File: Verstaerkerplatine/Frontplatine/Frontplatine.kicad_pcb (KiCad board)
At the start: 2 copper layers, 99.1 x 99.1 mm, 38 parts, among them J1 GND, J10 IV_IN_+, J11 IV_OUT, J12 IV_REF, J13 AVS_IN_+, J14 AVS_IN_-, J16 A0, J17 A1, J18 A2, J19 A3, J20 GND, J21 -5V, J22 3.3V, J23 5V, J24 DI_IN_2, J25 DI_IN_1, J26 DI_OUT_3, J27 DI_OUT_2, J28 DI_OUT_1, J29 EM_20, J3 EM_OUT, J30 LED_20, J31 D/A_+, J32 5V_BUS, J33 3.3V_BUS, J34 EM_KOND, J4 GND_EM, J5 EM_IN, J6 PW_IN, J7 PW_OUT, J8 REF, J9 IV_IN_-

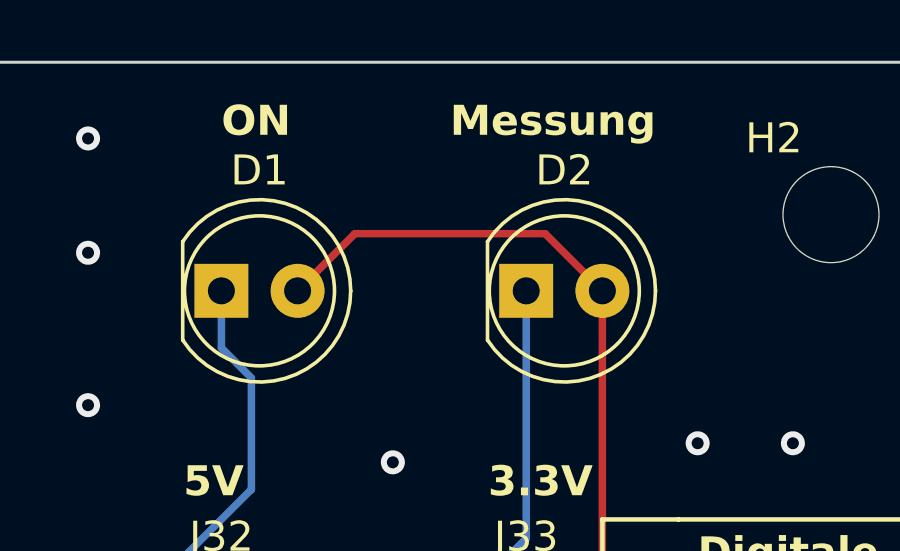
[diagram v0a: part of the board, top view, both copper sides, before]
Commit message: LED connection moved
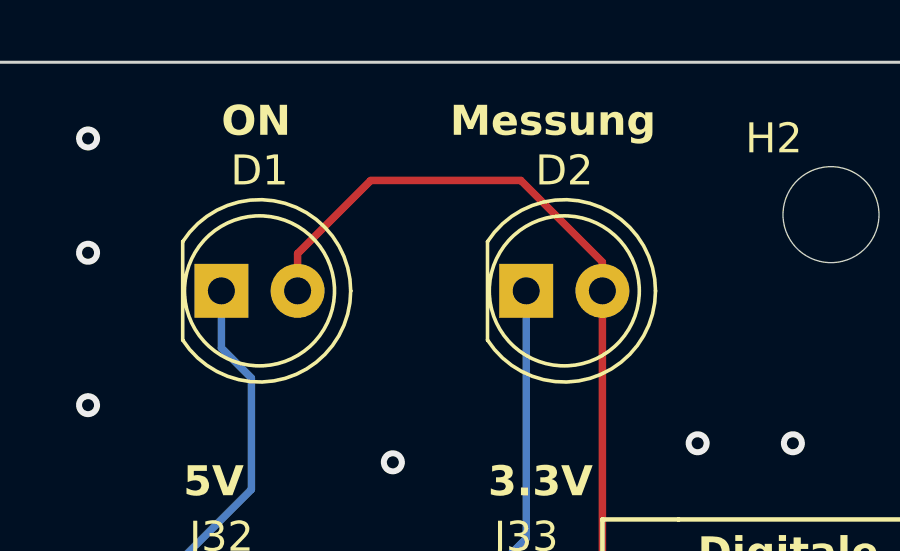
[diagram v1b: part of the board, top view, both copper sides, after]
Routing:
- net +3.3V: track 201.5 -> 204.3 mm
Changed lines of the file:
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@@
+	)
+	(segment
+		(start 165 39.5)
+		(end 170 39.5)
+		(width 0.25)
+		(layer "F.Cu")
+		(net 2)
 	)
 	(segment
@@
 	)
 	(segment
+		(start 170 39.5)
+		(end 172.72 42.22)
+		(width 0.25)
+		(layer "F.Cu")
+		(net 2)
+	)
+	(segment
 		(start 172.72 43.18)
 		(end 172.72 53.34)
@@
 	)
 	(segment
-		(start 164.465 41.275)
-		(end 170.815 41.275)
-		(width 0.25)
-		(layer "F.Cu")
-		(net 2)
-	)
-	(segment
-		(start 162.56 43.18)
-		(end 164.465 41.275)
-		(width 0.25)
-		(layer "F.Cu")
-		(net 2)
-	)
-	(segment
 		(start 171.45 85.725)
 		(end 171.45 57.15)
-		(width 0.25)
-		(layer "F.Cu")
-		(net 2)
-	)
-	(segment
-		(start 170.815 41.275)
-		(end 172.72 43.18)
 		(width 0.25)
 		(layer "F.Cu")
@@
 		(width 0.25)
 		(layer "F.Cu")
+		(net 2)
+	)
+	(segment
+		(start 172.72 42.22)
+		(end 172.72 43.18)
+		(width 0.25)
+		(layer "F.Cu")
+		(net 2)
+	)
+	(segment
+		(start 162.56 41.94)
+		(end 165 39.5)
+		(width 0.25)
+		(layer "F.Cu")
+		(net 2)
+	)
+	(segment
+		(start 162.56 43.18)
+		(end 162.56 41.94)
+		(width 0.25)
+		(layer "F.Cu")

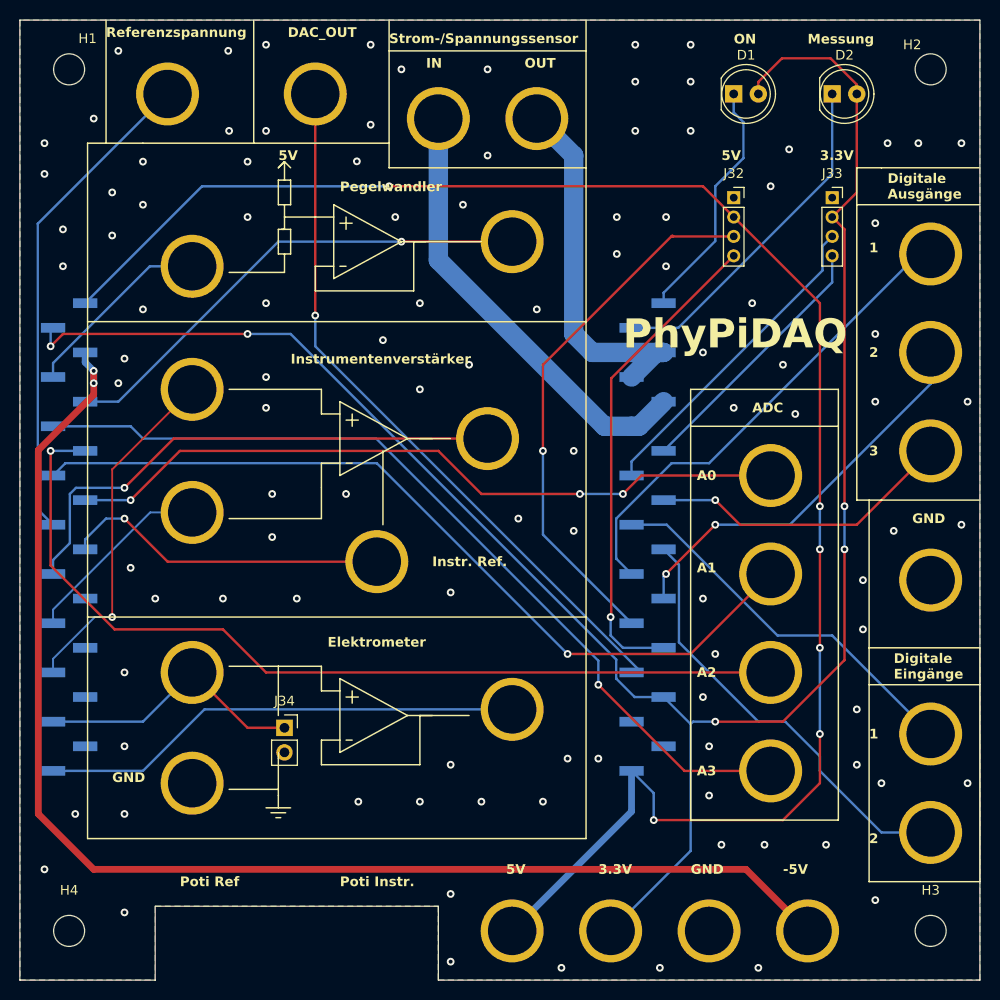
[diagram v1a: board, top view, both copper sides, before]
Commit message: wired connection for CA3140 in and IN219 IN+ and IN-
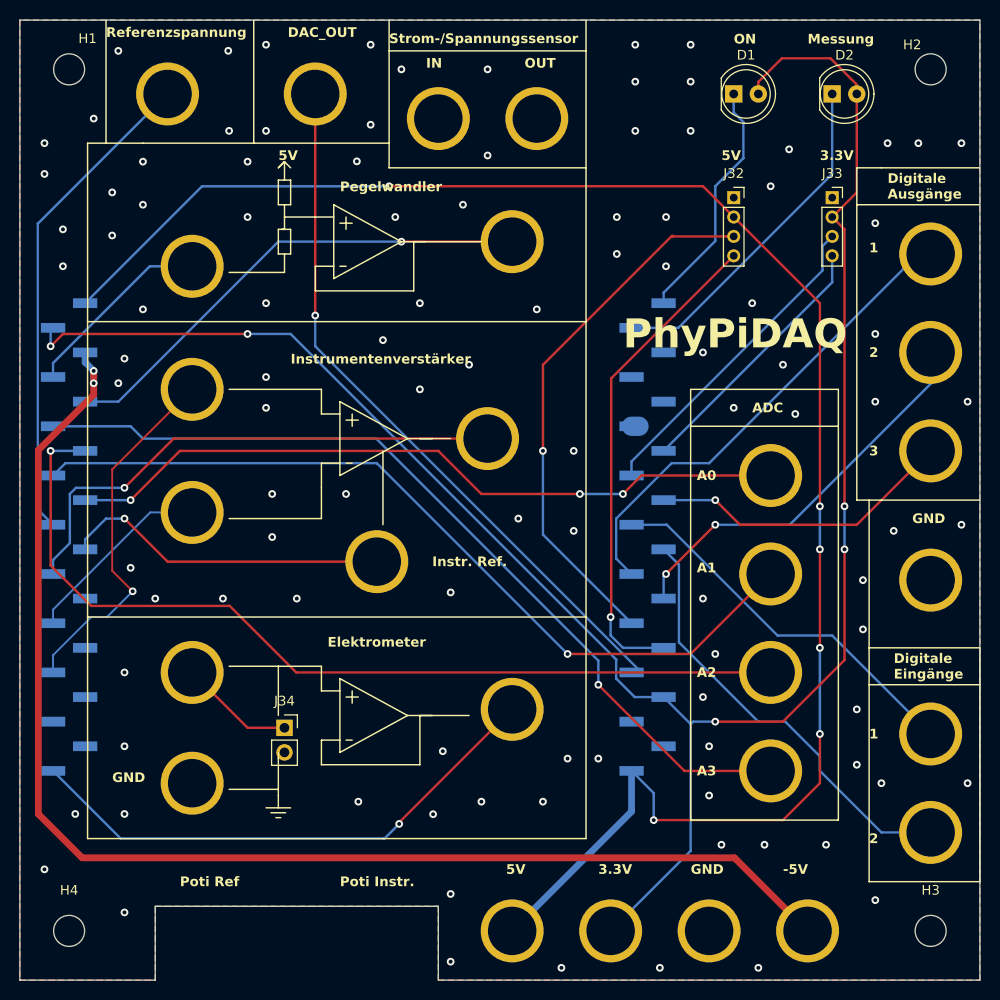
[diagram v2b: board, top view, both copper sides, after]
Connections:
- J13 pad 1: StromSpannungsSensor_IN_+ -> unconnected-(J13-Pin_1-Pad1)
- J14 pad 1: StromSpannungsSensor_IN_- -> unconnected-(J14-Pin_1-Pad1)
- J29 pad 3: Elektrometer_IN_+ -> unconnected-(J29-Pin_3-Pad3)
- J30 pad 3: StromSpannungsSensor_IN_- -> unconnected-(J30-Pin_3-Pad3)
- J30 pad 4: StromSpannungsSensor_IN_- -> unconnected-(J30-Pin_4-Pad4)
- J30 pad 5: StromSpannungsSensor_IN_+ -> unconnected-(J30-Pin_5-Pad5)
- J30 pad 6: StromSpannungsSensor_IN_+ -> unconnected-(J30-Pin_6-Pad6)
- J34 pad 1: Elektrometer_IN_+ -> Net-(J34-Pin_1)
- J5 pad 1: Elektrometer_IN_+ -> Net-(J34-Pin_1)
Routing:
- net StromSpannungsSensor_IN_+: track 46.0 -> 0.00 mm
- net StromSpannungsSensor_IN_-: track 38.2 -> 0.00 mm
- net Elektrometer_IN_+: track 28.4 -> 0.00 mm
- net Net-(J34-Pin_1): track 0.00 -> 11.9 mm
- net Elektrometer_OUT: track 50.0 -> 55.9 mm, vias 0 -> 1
- net Instrumentenverstaerker_IN_+: track 36.2 -> 37.9 mm
- net unconnected-(J30-Pin_6-Pad6): track 0.00 -> 0.77 mm
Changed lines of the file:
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@@
 	(net 4 "GND")
 	(net 5 "Elektrometer_OUT")
-	(net 6 "Elektrometer_IN_+")
+	(net 6 "Net-(J34-Pin_1)")
 	(net 7 "Pegelwandler_IN_+")
 	(net 8 "Pegelwandler_OUT")
@@
 	(net 12 "Instrumentenverstaerker_OUT")
 	(net 13 "Instrumentenverstaerker_Ref")
-	(net 14 "StromSpannungsSensor_IN_+")
-	(net 15 "StromSpannungsSensor_IN_-")
+	(net 14 "unconnected-(J13-Pin_1-Pad1)")
+	(net 15 "unconnected-(J14-Pin_1-Pad1)")
 	(net 16 "A0")
 	(net 17 "A1")
@@
 	(net 30 "SCL_5")
 	(net 31 "DAC_OUT")
+	(net 32 "unconnected-(J29-Pin_3-Pad3)")
+	(net 33 "unconnected-(J30-Pin_5-Pad5)")
+	(net 34 "unconnected-(J30-Pin_4-Pad4)")
+	(net 35 "unconnected-(J30-Pin_3-Pad3)")
+	(net 36 "unconnected-(J30-Pin_6-Pad6)")
 	(footprint "MountingHole:MountingHole_3.2mm_M3"
 		(layer "F.Cu")
@@
 			(layers "*.Cu" "*.Mask")
 			(remove_unused_layers no)
-			(net 6 "Elektrometer_IN_+")
+			(net 6 "Net-(J34-Pin_1)")
 			(pinfunction "Pin_1")
 			(pintype "passive")
@@
 			(layers "*.Cu" "*.Mask")
 			(remove_unused_layers no)
-			(net 14 "StromSpannungsSensor_IN_+")
+			(net 14 "unconnected-(J13-Pin_1-Pad1)")
 			(pinfunction "Pin_1")
 			(pintype "passive")
@@
 			(layers "*.Cu" "*.Mask")
 			(remove_unused_layers no)
-			(net 6 "Elektrometer_IN_+")
+			(net 6 "Net-(J34-Pin_1)")
 			(pinfunction "Pin_1")
 			(pintype "passive")
@@
 			(size 2.51 1)
 			(layers "B.Cu" "B.Mask" "B.Paste")
-			(net 6 "Elektrometer_IN_+")
+			(net 32 "unconnected-(J29-Pin_3-Pad3)")
 			(pinfunction "Pin_3")
-			(pintype "passive")
+			(pintype "passive+no_connect")
 		)
 		(pad "4" smd rect
@@
 			(layers "*.Cu" "*.Mask")
 			(remove_unused_layers no)
-			(net 15 "StromSpannungsSensor_IN_-")
+			(net 15 "unconnected-(J14-Pin_1-Pad1)")
 			(pinfunction "Pin_1")
 			(pintype "passive")
@@
 			(size 2.51 1)
 			(layers "B.Cu" "B.Mask" "B.Paste")
-			(net 15 "StromSpannungsSensor_IN_-")
+			(net 35 "unconnected-(J30-Pin_3-Pad3)")
 			(pinfunction "Pin_3")
-			(pintype "passive")
+			(pintype "passive+no_connect")
 		)
 		(pad "4" smd rect
@@
 			(size 2.51 1)
 			(layers "B.Cu" "B.Mask" "B.Paste")
-			(net 15 "StromSpannungsSensor_IN_-")
+			(net 34 "unconnected-(J30-Pin_4-Pad4)")
 			(pinfunction "Pin_4")
-			(pintype "passive")
+			(pintype "passive+no_connect")
 		)
 		(pad "5" smd rect
@@
 			(size 2.51 1)
 			(layers "B.Cu" "B.Mask" "B.Paste")
-			(net 14 "StromSpannungsSensor_IN_+")
+			(net 33 "unconnected-(J30-Pin_5-Pad5)")
 			(pinfunction "Pin_5")
-			(pintype "passive")
+			(pintype "passive+no_connect")
 		)
 		(pad "6" smd rect
@@
 			(size 2.51 1)
 			(layers "B.Cu" "B.Mask" "B.Paste")
-			(net 14 "StromSpannungsSensor_IN_+")
+			(net 36 "unconnected-(J30-Pin_6-Pad6)")
 			(pinfunction "Pin_6")
-			(pintype "passive")
+			(pintype "passive+no_connect")
 		)
 		(pad "7" smd rect
@@
 	)
 	(via
-		(at 127.635 116.205)
+		(at 129 117.5)
 		(size 0.8)
 		(drill 0.4)
@@
 	)
 	(via
-		(at 130.81 112.395)
+		(at 130 111)
 		(size 0.8)
 		(drill 0.4)
@@
 	)
 	(segment
-		(start 99.06 113.03)
-		(end 105.41 106.68)
+		(start 125.5 118.5)
+		(end 125.5 118.34)
 		(width 0.25)
-		(layer "B.Cu")
+		(layer "F.Cu")
 		(net 5)
 	)
 	(segment
-		(start 105.41 106.68)
+		(start 125.5 118.34)
 		(end 137.16 106.68)
 		(width 0.25)
+		(layer "F.Cu")
+		(net 5)
+	)
+	(via
+		(at 125.5 118.5)
+		(size 0.8)
+		(drill 0.4)
+		(layers "F.Cu" "B.Cu")
+		(net 5)
+	)
+	(segment
+		(start 124 120)
+		(end 125.5 118.5)
+		(width 0.25)
+		(layer "B.Cu")
+		(net 5)
+	)
+	(segment
+		(start 96.755 120)
+		(end 123.84 120)
+		(width 0.25)
+		(layer "B.Cu")
+		(net 5)
+	)
+	(segment
+		(start 123.84 120)
+		(end 124 120)
+		(width 0.25)
 		(layer "B.Cu")
 		(net 5)
@@
 	(segment
 		(start 89.785 113.03)
-		(end 99.06 113.03)
+		(end 96.755 120)
 		(width 0.25)
 		(layer "B.Cu")
@@
 	)
 	(segment
-		(start 89.785 107.95)
-		(end 99.06 107.95)
-		(width 0.25)
-		(layer "B.Cu")
-		(net 6)
-	)
-	(segment
-		(start 99.06 107.95)
-		(end 104.14 102.87)
-		(width 0.25)
-		(layer "B.Cu")
-		(net 6)
-	)
-	(segment
 		(start 89.785 72.39)
 		(end 89.785 70.94538)
@@
 	)
 	(segment
-		(start 104.14 73.66)
+		(start 95.885 92.385)
 		(end 95.885 81.915)
 		(width 0.2)
@@
 	)
 	(segment
+		(start 98 94.5)
+		(end 95.885 92.385)
+		(width 0.2)
+		(layer "F.Cu")
+		(net 11)
+	)
+	(segment
 		(start 95.885 81.915)
-		(end 95.885 97.155)
+		(end 104.14 73.66)
 		(width 0.2)
 		(layer "F.Cu")
@@
 	)
 	(via
-		(at 95.885 97.155)
+		(at 98 94.5)
 		(size 0.8)
 		(drill 0.4)
@@
 	)
 	(segment
-		(start 95.885 97.155)
-		(end 94.090736 97.155)
+		(start 95.345 97.155)
+		(end 93.717868 97.155)
 		(width 0.2)
 		(layer "B.Cu")
@@
 	)
 	(segment
-		(start 89.785 101.460736)
-		(end 89.785 102.87)
+		(start 93.717868 97.155)
+		(end 89.785 101.087868)
 		(width 0.2)
 		(layer "B.Cu")
@@
 	)
 	(segment
-		(start 94.090736 97.155)
-		(end 89.785 101.460736)
+		(start 98 94.5)
+		(end 95.345 97.155)
+		(width 0.2)
+		(layer "B.Cu")
+		(net 11)
+	)
+	(segment
+		(start 89.785 101.087868)
+		(end 89.785 102.87)
 		(width 0.2)
 		(layer "B.Cu")
@@
 	)
 	(segment
-		(start 149.475 77.47)
-		(end 150.245 77.47)
-		(width 2)
-		(layer "B.Cu")
-		(net 14)
-	)
-	(segment
-		(start 146.685 77.47)
-		(end 129.54 60.325)
-		(width 2)
-		(layer "B.Cu")
-		(net 14)
-	)
-	(segment
-		(start 150.245 77.47)
-		(end 152.785 74.93)
-		(width 2)
-		(layer "B.Cu")
-		(net 14)
-	)
-	(segment
-		(start 149.475 77.47)
-		(end 146.685 77.47)
-		(width 2)
-		(layer "B.Cu")
-		(net 14)
-	)
-	(segment
-		(start 129.54 60.325)
-		(end 129.54 45.72)
-		(width 2)
-		(layer "B.Cu")
-		(net 14)
-	)
-	(segment
-		(start 152.015 69.85)
-		(end 149.475 72.39)
-		(width 2)
-		(layer "B.Cu")
-		(net 15)
-	)
-	(segment
-		(start 145.415 69.85)
-		(end 143.51 67.945)
-		(width 2)
-		(layer "B.Cu")
-		(net 15)
-	)
-	(segment
-		(start 152.785 69.85)
-		(end 145.415 69.85)
-		(width 2)
-		(layer "B.Cu")
-		(net 15)
-	)
-	(segment
-		(start 143.51 67.945)
-		(end 143.51 49.53)
-		(width 2)
-		(layer "B.Cu")
-		(net 15)
-	)
-	(segment
-		(start 152.785 69.85)
-		(end 152.015 69.85)
-		(width 2)
-		(layer "B.Cu")
-		(net 15)
-	)
-	(segment
-		(start 143.51 49.53)
-		(end 139.7 45.72)
-		(width 2)
-		(layer "B.Cu")
-		(net 15)
-	)
-	(segment
 		(start 97.79 85.09)
 		(end 102.87 80.01)
@@
 	)
 	(segment
-		(start 89.535 91.830305)
-		(end 89.535 80.01)
+		(start 108 96)
+		(end 93.704695 96)
 		(width 0.25)
 		(layer "F.Cu")
@@
 	)
 	(segment
-		(start 96.129695 98.425)
+		(start 93.704695 96)
 		(end 89.535 91.830305)
 		(width 0.25)
@@
 	)
 	(segment
-		(start 111.76 102.87)
-		(end 107.315 98.425)
+		(start 89.535 91.830305)
+		(end 89.535 80.01)
 		(width 0.25)
 		(layer "F.Cu")
@@
 	)
 	(segment
-		(start 163.83 102.87)
-		(end 111.76 102.87)
+		(start 114.87 102.87)
+		(end 108 96)
 		(width 0.25)
 		(layer "F.Cu")
@@
 	)
 	(segment
-		(start 107.315 98.425)
-		(end 96.129695 98.425)
+		(start 163.83 102.87)
+		(end 114.87 102.87)
 		(width 0.25)
 		(layer "F.Cu")
@@
 	)
 	(segment
-		(start 161.29 123.19)
+		(start 160.1 122)
 		(end 167.64 129.54)
 		(width 0.7)
@@
 	)
 	(segment
-		(start 88.265 79.936497)
-		(end 88.265 117.475)
+		(start 93.98 74.221497)
+		(end 88.265 79.936497)
 		(width 0.7)
 		(layer "F.Cu")
@@
 	)
 	(segment
-		(start 93.98 71.755)
-		(end 93.98 74.221497)
+		(start 92.79 122)
+		(end 160.1 122)
 		(width 0.7)
 		(layer "F.Cu")
@@
 	)
 	(segment
-		(start 93.98 123.19)
-		(end 161.29 123.19)
+		(start 93.98 71.755)
+		(end 93.98 74.221497)
 		(width 0.7)
 		(layer "F.Cu")
@@
 	)
 	(segment
-		(start 93.98 74.221497)
-		(end 88.265 79.936497)
+		(start 88.265 117.475)
+		(end 92.79 122)
 		(width 0.7)
 		(layer "F.Cu")
@@
 	)
 	(segment
-		(start 88.265 117.475)
-		(end 93.98 123.19)
+		(start 88.265 79.936497)
+		(end 88.265 117.475)
 		(width 0.7)
 		(layer "F.Cu")
@@
 		(net 31)
 	)
+	(segment
+		(start 149.475 77.47)
+		(end 150.245 77.47)
+		(width 2)
+		(layer "B.Cu")
+		(net 36)
+	)
 	(zone
